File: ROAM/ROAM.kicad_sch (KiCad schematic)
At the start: 11 parts, among them J1 CommanderX16Expansion Alt, U1 SST39SF040 (ROM), U2 74HCT00, U3 74HCT138, U4 AS6C4008 (RAM)

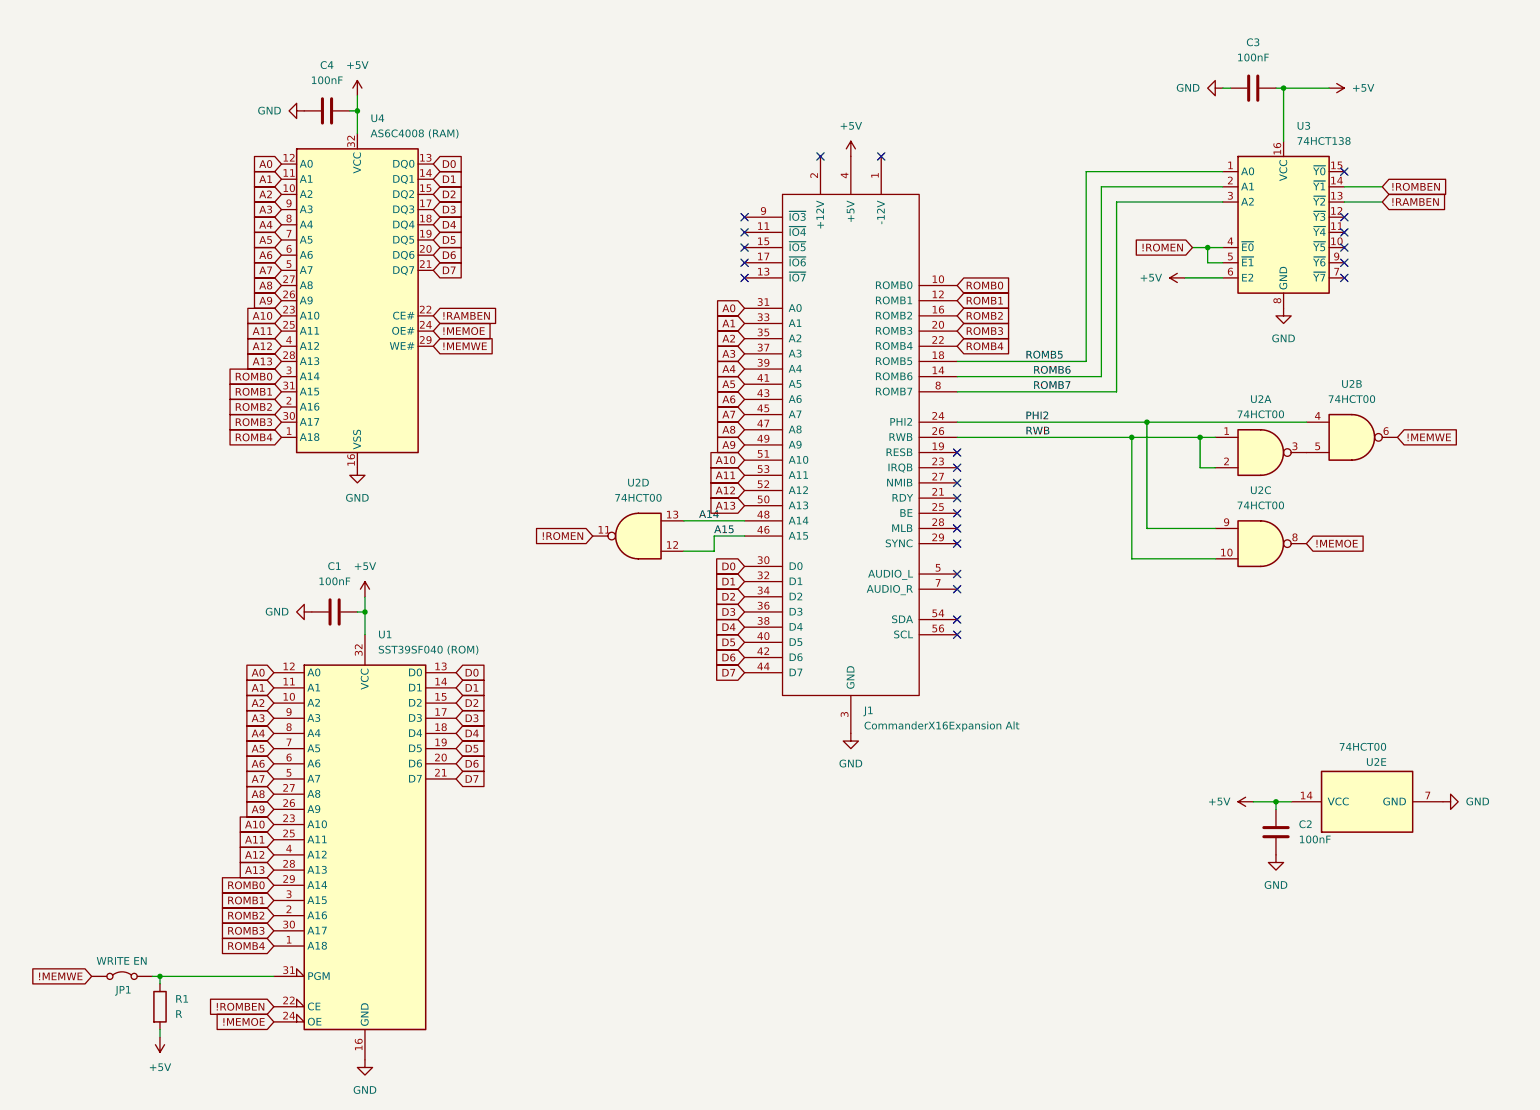
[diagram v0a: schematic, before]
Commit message: Merged Wavicle's contributions to ROAM, added silk and some markup, updated readmed
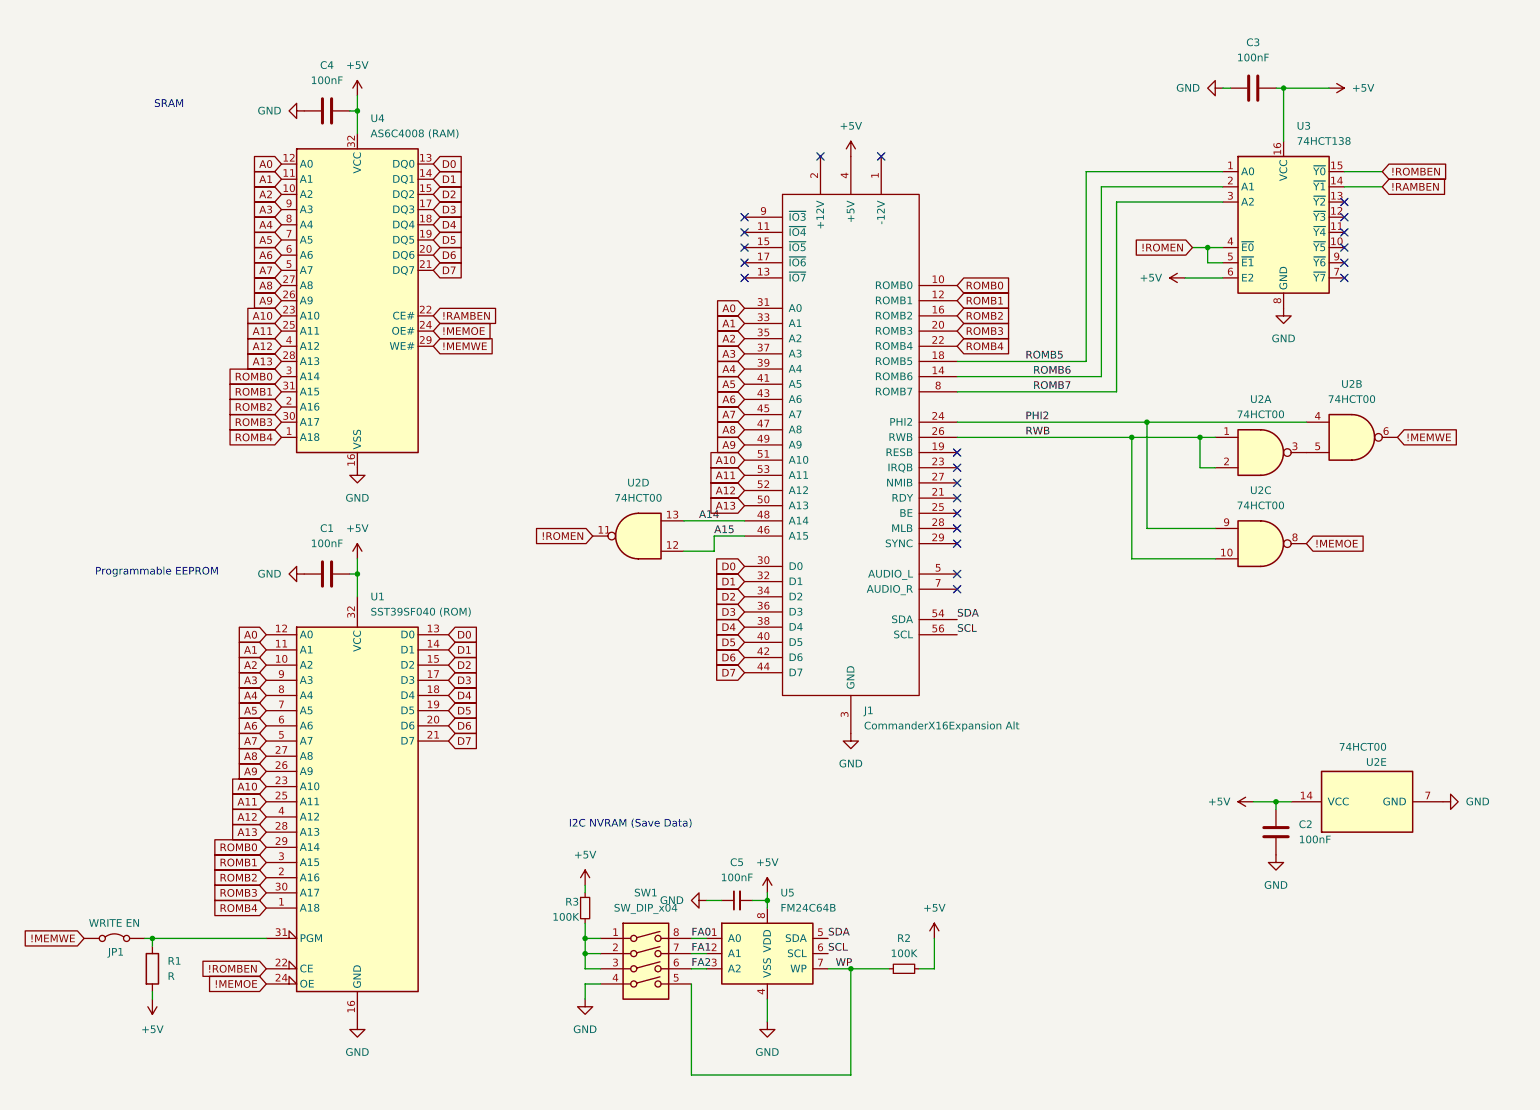
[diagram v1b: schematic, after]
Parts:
- added C5: 100nF, Capacitor_THT:C_Axial_L3.8mm_D2.6mm_P7.50mm_Horizontal, symbol Device:C_Small
- added R2, R3: 100K, Resistor_THT:R_Axial_DIN0204_L3.6mm_D1.6mm_P5.08mm_Horizontal, symbol Device:R_Small
- added SW1: SW_DIP_x04, Button_Switch_THT:SW_DIP_SPSTx04_Slide_9.78x12.34mm_W7.62mm_P2.54mm, symbol Switch:SW_DIP_x04
- added U5: FM24C64B, Package_SO:SOIC-8_3.9x4.9mm_P1.27mm, symbol Memory_NVRAM:FM24C64B
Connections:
- net !RAMBEN: now also U3.14 (~{Y1}); no longer U3.13 (~{Y2})
- net !ROMBEN: now also U3.15 (~{Y0}); no longer U3.14 (~{Y1})
- net +5V: now also C5.2, R2.2, R3.1, U5.8 (VDD)
- net GND: now also C5.1, SW1.4, U5.4 (VSS)
- net SDA: now reaches J1.54 (SDA)
- net SDA: now also U5.5 (SDA)
- net SCL: now reaches J1.56 (SCL)
- net SCL: now also U5.6 (SCL)
- new net: R3.2, SW1.1, SW1.2, SW1.3
- new net FA0: SW1.8, U5.1 (A0)
- new net FA1: SW1.7, U5.2 (A1)
- new net FA2: SW1.6, U5.3 (A2)
- new net WP: R2.1, SW1.5, U5.7 (WP)
- no-connect marks 24 -> 22
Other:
- note added: "I2C NVRAM (Save Data)"
- note added: "Programmable EEPROM"
- note added: "SRAM"
- moved on the sheet: C1, JP1, R1, U1

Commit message: Ported over Wavicle's latest changes
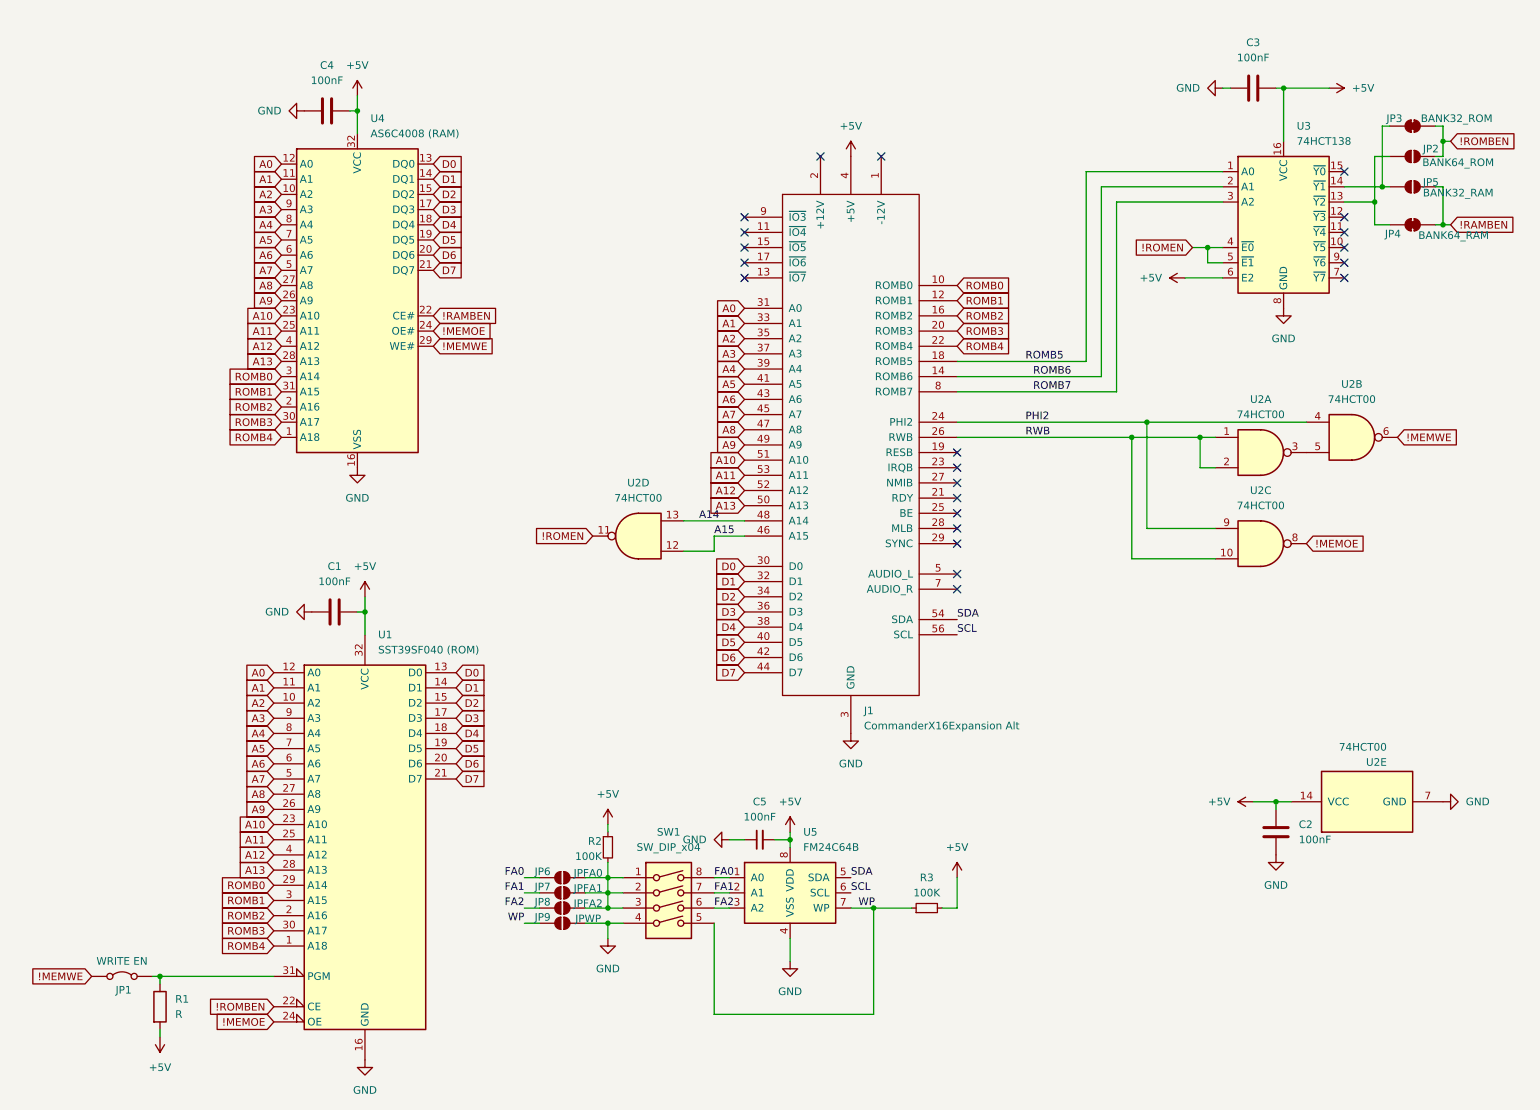
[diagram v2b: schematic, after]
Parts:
- removed J1: CommanderX16Expansion Alt, CommanderX16Expansion:CommanderX16Cartridge, symbol CommanderX16Expansion:CommanderX16Expansion Alt
- added J1: CommanderX16Expansion Alt, X16Expansion:CommanderX16Cartridge, symbol X16_Expansion:CommanderX16Expansion Alt
- added JP2: BANK64_ROM, Jumper:SolderJumper-2_P1.3mm_Open_TrianglePad1.0x1.5mm, symbol Jumper:SolderJumper_2_Open
- added JP3: BANK32_ROM, Jumper:SolderJumper-2_P1.3mm_Bridged_Pad1.0x1.5mm, symbol Jumper:SolderJumper_2_Bridged
- added JP4: BANK64_RAM, Jumper:SolderJumper-2_P1.3mm_Bridged_Pad1.0x1.5mm, symbol Jumper:SolderJumper_2_Bridged
- added JP5: BANK32_RAM, Jumper:SolderJumper-2_P1.3mm_Open_TrianglePad1.0x1.5mm, symbol Jumper:SolderJumper_2_Open
- added JP6: JPFA0, Jumper:SolderJumper-2_P1.3mm_Open_TrianglePad1.0x1.5mm, symbol Jumper:SolderJumper_2_Open
- added JP7: JPFA1, Jumper:SolderJumper-2_P1.3mm_Open_TrianglePad1.0x1.5mm, symbol Jumper:SolderJumper_2_Open
- added JP8: JPFA2, Jumper:SolderJumper-2_P1.3mm_Open_TrianglePad1.0x1.5mm, symbol Jumper:SolderJumper_2_Open
- added JP9: JPWP, Jumper:SolderJumper-2_P1.3mm_Open_TrianglePad1.0x1.5mm, symbol Jumper:SolderJumper_2_Open
- C1, C2, C3, C4, C5: footprint Capacitor_THT:C_Axial_L3.8mm_D2.6mm_P7.50mm_Horizontal -> Capacitor_THT:C_Disc_D4.3mm_W1.9mm_P5.00mm
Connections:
- net !RAMBEN: now also JP4.2 (B), JP5.1 (A); no longer U3.14 (~{Y1})
- net !ROMBEN: now also JP2.1 (A), JP3.2 (B); no longer U3.15 (~{Y0})
- net +5V: now also R2.1, R3.2, J1.4 (+5V), J1.57 (+5V); no longer R2.2, R3.1
- net A0: now also J1.31 (A0)
- net A1: now also J1.33 (A1)
- net A10: now also J1.51 (A10)
- net A11: now also J1.53 (A11)
- net A12: now also J1.52 (A12)
- net A13: now also J1.50 (A13)
- net A14: now also J1.48 (A14)
- net A15: now also J1.46 (A15)
- net A2: now also J1.35 (A2)
- net A3: now also J1.37 (A3)
- net A4: now also J1.39 (A4)
- net A5: now also J1.41 (A5)
- net A6: now also J1.43 (A6)
- net A7: now also J1.45 (A7)
- net A8: now also J1.47 (A8)
- net A9: now also J1.49 (A9)
- net D0: now also J1.30 (D0)
- net D1: now also J1.32 (D1)
- net D2: now also J1.34 (D2)
- net D3: now also J1.36 (D3)
- net D4: now also J1.38 (D4)
- net D5: now also J1.40 (D5)
- net D6: now also J1.42 (D6)
- net D7: now also J1.44 (D7)
- net FA0: now also JP6.2 (B)
- net FA1: now also JP7.2 (B)
- net FA2: now also JP8.2 (B)
- net GND: now also J1.3 (GND), J1.55 (GND), J1.58 (GND), J1.6 (GND), JP9.1 (A)
- net PHI2: now also J1.24 (PHI2)
- net ROMB0: now also J1.10 (ROMB0)
- net ROMB1: now also J1.12 (ROMB1)
- net ROMB2: now also J1.16 (ROMB2)
- net ROMB3: now also J1.20 (ROMB3)
- net ROMB4: now also J1.22 (ROMB4)
- net ROMB5: now also J1.18 (ROMB5)
- net ROMB6: now also J1.14 (ROMB6)
- net ROMB7: now also J1.8 (ROMB7)
- net RWB: now also J1.26 (RWB)
- net SCL: now also J1.56 (SCL)
- net SDA: now also J1.54 (SDA)
- net WP: now also R3.1, JP9.2 (B); no longer R2.1
- net at U3.13 (~{Y2}): now also JP2.2 (B), JP4.1 (A)
- net at SW1.1, SW1.2, SW1.3: now also R2.2, JP6.1 (A), JP7.1 (A), JP8.1 (A); no longer R3.2
- new net: JP3.1 (A), JP5.2 (B), U3.14 (~{Y1})
- new net: J1.1 (-12V), J1.60 (-12V)
- new net: J1.2 (+12V), J1.59 (+12V)
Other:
- note removed: "I2C NVRAM (Save Data)"
- note removed: "Programmable EEPROM"
- note removed: "SRAM"
- moved on the sheet: C1, JP1, R1, U1

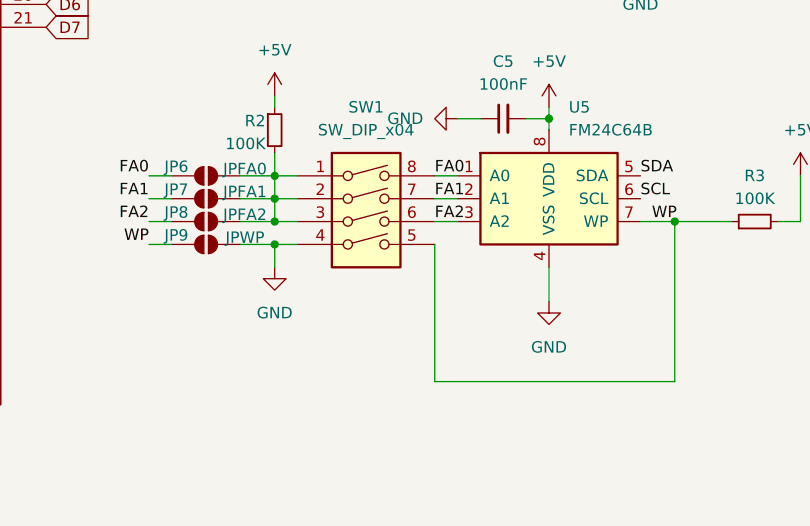
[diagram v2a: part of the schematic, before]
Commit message: Added label about pull-downs, updates to readme
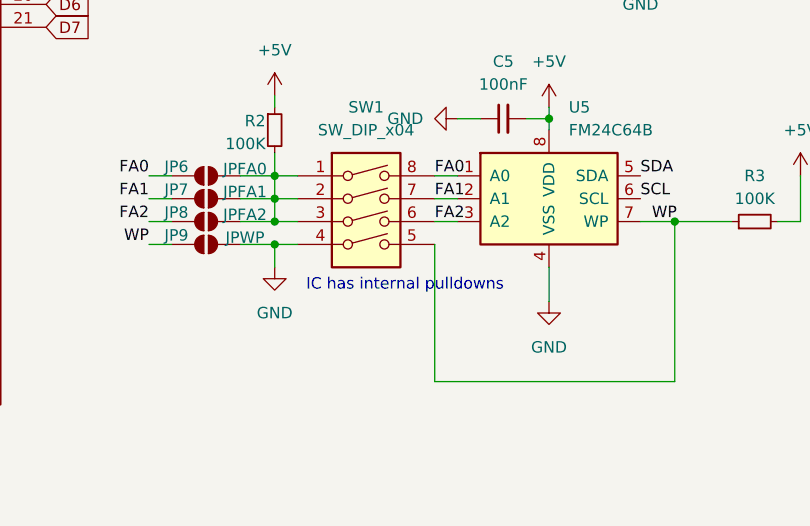
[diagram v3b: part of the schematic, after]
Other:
- note added: "IC has internal pulldowns"
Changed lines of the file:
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@@
+		)
+	)
+	(text "IC has internal pulldowns"
+		(exclude_from_sim no)
+		(at 128.778 170.942 0)
+		(effects
+			(font
+				(size 1.27 1.27)
+			)
 		)
 	)

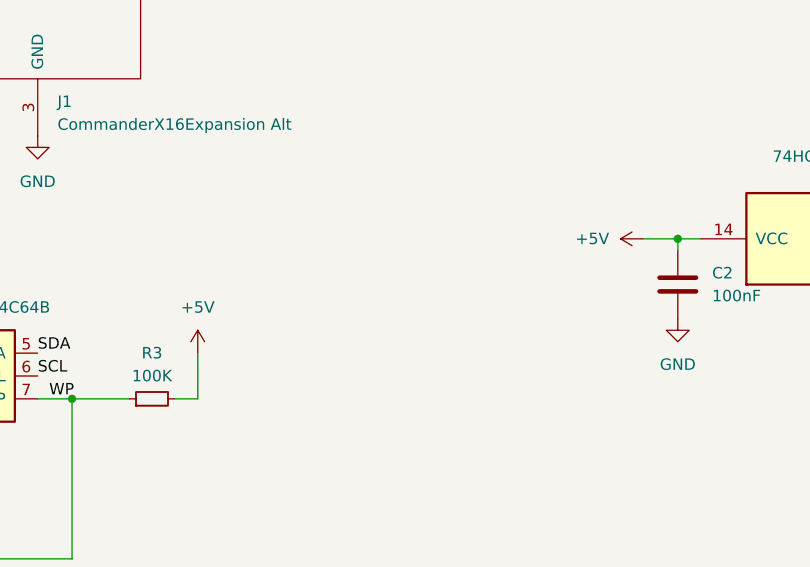
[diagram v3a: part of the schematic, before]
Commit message: 1uF Caps
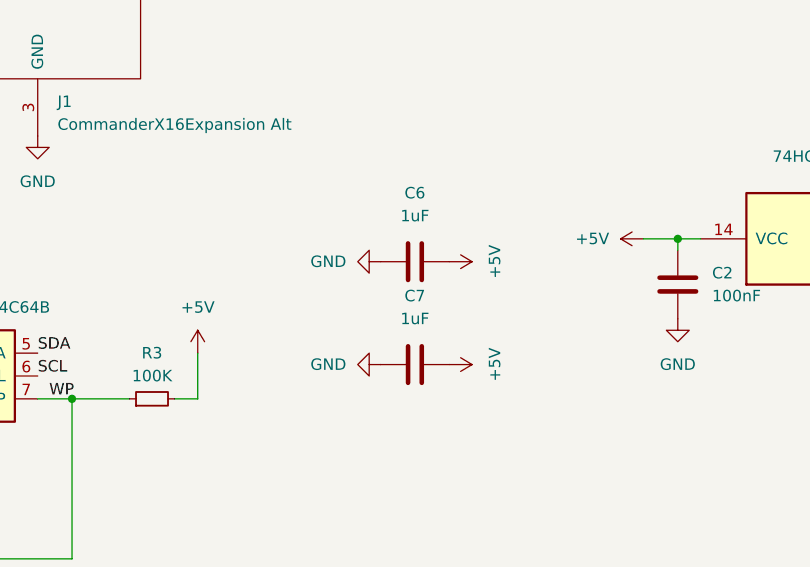
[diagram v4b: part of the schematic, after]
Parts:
- added C6, C7: 1uF, Capacitor_THT:C_Disc_D4.3mm_W1.9mm_P5.00mm, symbol Device:C
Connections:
- net +5V: now also C6.2, C7.2
- net GND: now also C6.1, C7.1

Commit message: Time to buy!
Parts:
- R1, R2, R3: footprint Resistor_THT:R_Axial_DIN0204_L3.6mm_D1.6mm_P5.08mm_Horizontal -> Resistor_THT:R_Axial_DIN0204_L3.6mm_D1.6mm_P7.62mm_Horizontal
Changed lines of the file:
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@@
 			)
 		)
-		(property "Footprint" "Resistor_THT:R_Axial_DIN0204_L3.6mm_D1.6mm_P5.08mm_Horizontal"
+		(property "Footprint" "Resistor_THT:R_Axial_DIN0204_L3.6mm_D1.6mm_P7.62mm_Horizontal"
 			(at 37.592 180.34 90)
 			(effects
@@
 			)
 		)
-		(property "Footprint" "Resistor_THT:R_Axial_DIN0204_L3.6mm_D1.6mm_P5.08mm_Horizontal"
+		(property "Footprint" "Resistor_THT:R_Axial_DIN0204_L3.6mm_D1.6mm_P7.62mm_Horizontal"
 			(at 167.64 163.83 0)
 			(effects
@@
 			)
 		)
-		(property "Footprint" "Resistor_THT:R_Axial_DIN0204_L3.6mm_D1.6mm_P5.08mm_Horizontal"
+		(property "Footprint" "Resistor_THT:R_Axial_DIN0204_L3.6mm_D1.6mm_P7.62mm_Horizontal"
 			(at 114.3 153.67 0)
 			(effects

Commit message: Routed new layout with larger footprint keepout zones.
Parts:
- U1: footprint Package_DIP:DIP-32_W15.24mm_Socket -> Socket:DIP_Socket-32_W11.9_W12.7_W15.24_W17.78_W18.5_3M_232-1285-00-0602J
- U2: footprint Package_DIP:DIP-14_W7.62mm_Socket -> Package_DIP:DIP-14_W7.62mm
- U3: footprint Package_DIP:DIP-16_W7.62mm_Socket -> Package_DIP:DIP-16_W7.62mm
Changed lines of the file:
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@@
 			)
 		)
-		(property "Footprint" "Package_DIP:DIP-16_W7.62mm_Socket"
+		(property "Footprint" "Package_DIP:DIP-16_W7.62mm"
 			(at 227.33 50.8 0)
 			(effects
@@
 			)
 		)
-		(property "Footprint" "Package_DIP:DIP-14_W7.62mm_Socket"
+		(property "Footprint" "Package_DIP:DIP-14_W7.62mm"
 			(at 223.52 87.63 0)
 			(effects
@@
 			)
 		)
-		(property "Footprint" "Package_DIP:DIP-32_W15.24mm_Socket"
+		(property "Footprint" "Socket:DIP_Socket-32_W11.9_W12.7_W15.24_W17.78_W18.5_3M_232-1285-00-0602J"
 			(at 73.66 147.32 0)
 			(effects
@@
 			)
 		)
-		(property "Footprint" "Package_DIP:DIP-14_W7.62mm_Socket"
+		(property "Footprint" "Package_DIP:DIP-14_W7.62mm"
 			(at 241.3 146.05 0)
 			(effects
@@
 			)
 		)
-		(property "Footprint" "Package_DIP:DIP-14_W7.62mm_Socket"
+		(property "Footprint" "Package_DIP:DIP-14_W7.62mm"
 			(at 238.76 85.09 0)
 			(effects
@@
 			)
 		)
-		(property "Footprint" "Package_DIP:DIP-14_W7.62mm_Socket"
+		(property "Footprint" "Package_DIP:DIP-14_W7.62mm"
 			(at 119.38 101.6 0)
 			(effects
@@
 			)
 		)
-		(property "Footprint" "Package_DIP:DIP-14_W7.62mm_Socket"
+		(property "Footprint" "Package_DIP:DIP-14_W7.62mm"
 			(at 223.52 102.87 0)
 			(effects

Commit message: Add ROM reverse polarity circuit; Gerber out 0.20
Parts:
- added D1: Overcurrent, LED_THT:LED_D3.0mm, symbol Device:LED
- added F1: 250mA hold / 500mA trip, Fuse:Fuse_Bourns_MF-RHT100, symbol Device:Polyfuse_Small
- added R4: 4K7, Resistor_THT:R_Axial_DIN0204_L3.6mm_D1.6mm_P7.62mm_Horizontal, symbol Device:R_Small
- R1: value R -> 47K
- SW1: MPN (none) -> Wurth 418117270904
- U1: MPN (none) -> Microchip SST39SF040-70-4C-PHE
- U2: MPN (none) -> TI SN74AHC00N
- U3: MPN (none) -> TI SN74AHC138N
- U4: MPN (none) -> Alliance AS6C4008-55PCN
- U5: MPN (none) -> Infineon FM24C64B-G
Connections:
- net +5V: no longer C1.2, C4.2, C7.2, J1.57 (+5V), U1.32 (VCC), U4.32 (VCC)
- new net: D1.2 (A), R4.1
- new net: F1.2, J1.57 (+5V), R4.2
- new net +5VD: C1.2, C4.2, C7.2, D1.1 (K), F1.1, U1.32 (VCC), U4.32 (VCC)
